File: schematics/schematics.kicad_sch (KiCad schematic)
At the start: 3 parts, among them J1 ODU Diagnostic Port, J2 3.3V-5V Level Shifter, J3 XIAO ESP32C3

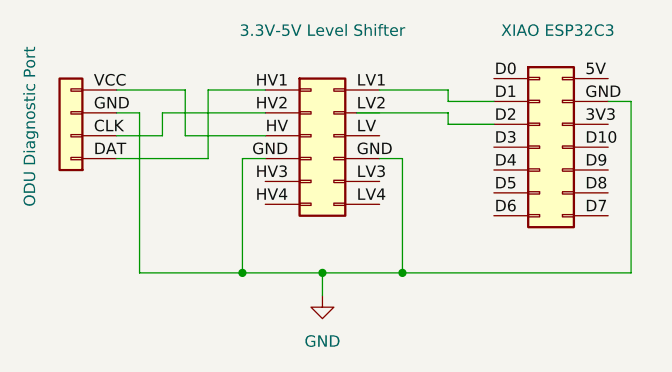
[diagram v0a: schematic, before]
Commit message: switch to HWCDCSerial
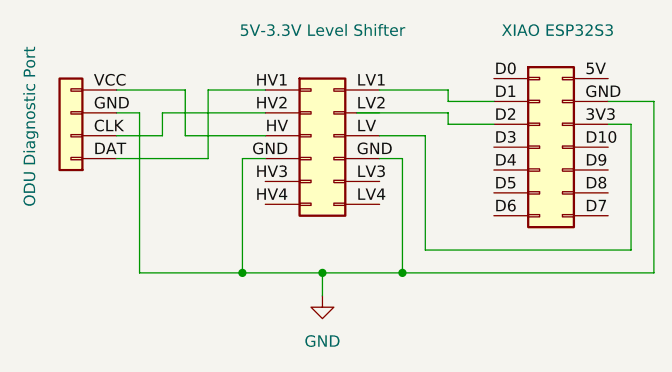
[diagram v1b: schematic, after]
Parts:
- J2: value 3.3V-5V Level Shifter -> 5V-3.3V Level Shifter
- J3: value XIAO ESP32C3 -> XIAO ESP32S3
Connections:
- net at J2.6 (Pin_6): now also J3.12 (Pin_12)
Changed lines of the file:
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@@
 	(wire
 		(pts
-			(xy 92.71 80.01) (xy 118.11 80.01)
+			(xy 92.71 80.01) (xy 120.65 80.01)
 		)
 		(stroke
@@
 	(wire
 		(pts
-			(xy 118.11 60.96) (xy 118.11 80.01)
+			(xy 120.65 60.96) (xy 120.65 80.01)
 		)
 		(stroke
@@
 	(wire
 		(pts
+			(xy 118.11 63.5) (xy 115.57 63.5)
+		)
+		(stroke
+			(width 0)
+			(type default)
+		)
+	)
+	(wire
+		(pts
 			(xy 83.82 80.01) (xy 83.82 82.55)
 		)
@@
 	(wire
 		(pts
+			(xy 118.11 77.47) (xy 118.11 63.5)
+		)
+		(stroke
+			(width 0)
+			(type default)
+		)
+	)
+	(wire
+		(pts
 			(xy 66.04 64.77) (xy 66.04 62.23)
 		)
@@
 	(wire
 		(pts
+			(xy 95.25 77.47) (xy 118.11 77.47)
+		)
+		(stroke
+			(width 0)
+			(type default)
+		)
+	)
+	(wire
+		(pts
+			(xy 95.25 64.77) (xy 95.25 77.47)
+		)
+		(stroke
+			(width 0)
+			(type default)
+		)
+	)
+	(wire
+		(pts
 			(xy 63.5 62.23) (xy 63.5 80.01)
 		)
@@
 	(wire
 		(pts
-			(xy 115.57 60.96) (xy 118.11 60.96)
+			(xy 115.57 60.96) (xy 120.65 60.96)
+		)
+		(stroke
+			(width 0)
+			(type default)
+		)
+	)
+	(wire
+		(pts
+			(xy 90.17 64.77) (xy 95.25 64.77)
 		)
 		(stroke
@@
 			)
 		)
-		(property "Value" "3.3V-5V Level Shifter"
+		(property "Value" "5V-3.3V Level Shifter"
 			(at 83.82 53.086 0)
 			(show_name no)
@@
 			)
 		)
-		(property "Value" "XIAO ESP32C3"
+		(property "Value" "XIAO ESP32S3"
 			(at 109.982 53.086 0)
 			(show_name no)
